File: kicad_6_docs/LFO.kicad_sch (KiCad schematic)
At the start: 13 parts, among them SW2 SW_SPDT, U14 SSI2164, U15 TL072

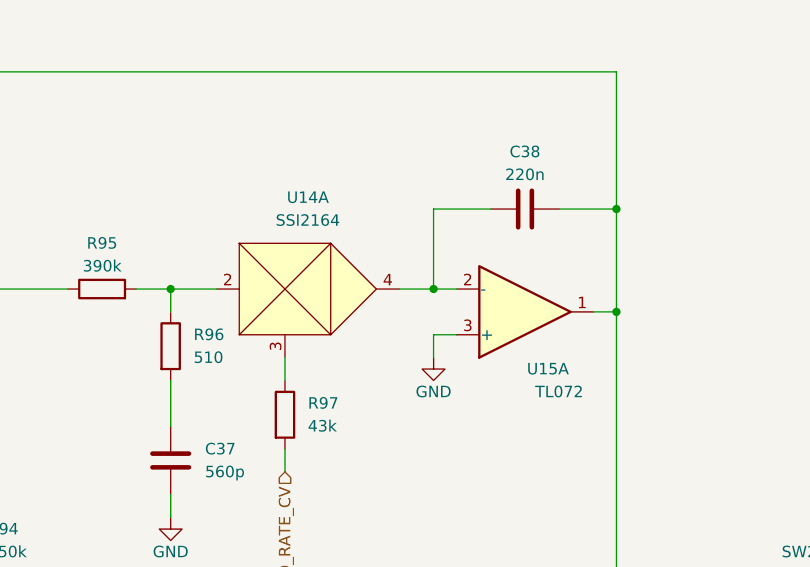
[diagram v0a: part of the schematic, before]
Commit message: Fix power supply errors, tidy up schematic
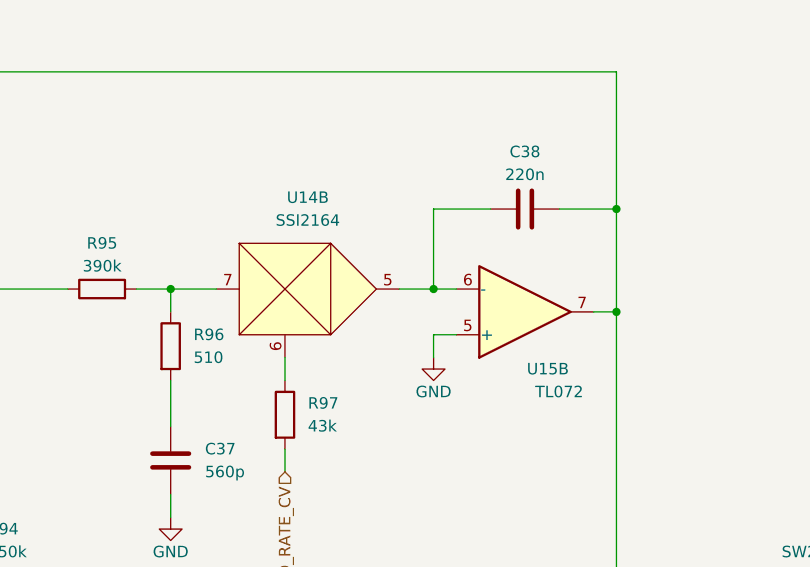
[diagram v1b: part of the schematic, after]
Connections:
- net GND: now also U15.5 (+); no longer U15.3 (+)
- net TRIANGLE: now also U15.7; no longer U15.1
- net at R97.1: now also U14.6; no longer U14.3
- net at R95.2, R96.1: now also U14.7; no longer U14.2
- new net: C38.1, U14.5, U15.6 (-)
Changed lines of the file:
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@@
   (title_block
     (title "Mu-Tron Bi-Phase near-clone")
-    (date "2022-01-14")
+    (date "2022-08-01")
     (rev "0")
     (comment 2 "creativecommons.org/licenses/by/4.0/")
@@
     (effects (font (size 1.27 1.27)) (justify left))
   )
-  (symbol (lib_id "Device:R") (at 148.59 101.6 0)
+  (symbol (lib_id "Device:R") (at 148.59 101.6 0) (unit 1)
     (in_bom yes) (on_board yes) (fields_autoplaced)
     (property "Reference" "R97" (id 0) (at 151.13 100.3299 0)
@@
     (pin "2")
   )
-  (symbol (lib_id "Amplifier_Operational:TL072") (at 175.26 90.17 0) (mirror x)
+  (symbol (lib_id "Amplifier_Operational:TL072") (at 175.26 90.17 0) (mirror x) (unit 2)
     (in_bom yes) (on_board yes)
     (property "Reference" "U15" (id 0) (at 177.8 96.52 0))
@@
       (effects (font (size 1.27 1.27)) hide)
     )
+    (pin "1")
+    (pin "2")
+    (pin "3")
     (pin "5")
     (pin "6")
     (pin "7")
-  )
-  (symbol (lib_id "Device:R") (at 96.52 76.2 90)
+    (pin "4")
+    (pin "8")
+  )
+  (symbol (lib_id "Device:R") (at 96.52 76.2 90) (unit 1)
     (in_bom yes) (on_board yes)
     (property "Reference" "R93" (id 0) (at 96.52 71.12 90))
@@
     (pin "2")
   )
-  (symbol (lib_id "custom_symbols:SSI2164") (at 148.59 87.63 0)
+  (symbol (lib_id "custom_symbols:SSI2164") (at 148.59 87.63 0) (unit 2)
     (in_bom yes) (on_board yes) (fields_autoplaced)
     (property "Reference" "U14" (id 0) (at 151.13 77.47 0))
@@
       (effects (font (size 1.27 1.27)) hide)
     )
+    (pin "2")
+    (pin "3")
+    (pin "4")
     (pin "5")
     (pin "6")
     (pin "7")
-  )
-  (symbol (lib_id "Device:C") (at 135.89 106.68 0)
+    (pin "10")
+    (pin "11")
+    (pin "12")
+    (pin "13")
+    (pin "14")
+    (pin "15")
+    (pin "1")
+    (pin "16")
+    (pin "8")
+    (pin "9")
+  )
+  (symbol (lib_id "Device:C") (at 135.89 106.68 0) (unit 1)
     (in_bom yes) (on_board yes) (fields_autoplaced)
     (property "Reference" "C37" (id 0) (at 139.7 105.4099 0)
@@
     (pin "2")
   )
-  (symbol (lib_id "Device:R") (at 113.03 115.57 0)
+  (symbol (lib_id "Device:R") (at 113.03 115.57 0) (unit 1)
     (in_bom yes) (on_board yes) (fields_autoplaced)
     (property "Reference" "R94" (id 0) (at 115.57 114.2999 0)
@@
     (pin "2")
   )
-  (symbol (lib_id "Device:C") (at 175.26 78.74 90)
+  (symbol (lib_id "Device:C") (at 175.26 78.74 90) (unit 1)
     (in_bom yes) (on_board yes)
     (property "Reference" "C38" (id 0) (at 175.26 72.39 90))
@@
     (pin "2")
   )
-  (symbol (lib_id "Device:C") (at 113.03 133.35 0)
+  (symbol (lib_id "Device:C") (at 113.03 133.35 0) (unit 1)
     (in_bom yes) (on_board yes) (fields_autoplaced)
     (property "Reference" "C36" (id 0) (at 116.84 132.0799 0)
@@
     (pin "2")
   )
-  (symbol (lib_id "Device:R") (at 135.89 93.98 0)
+  (symbol (lib_id "Device:R") (at 135.89 93.98 0) (unit 1)
     (in_bom yes) (on_board yes) (fields_autoplaced)
     (property "Reference" "R96" (id 0) (at 138.43 92.7099 0)
@@
     (pin "2")
   )
-  (symbol (lib_id "power:GND") (at 165.1 95.25 0)
+  (symbol (lib_id "power:GND") (at 165.1 95.25 0) (unit 1)
     (in_bom yes) (on_board yes)
     (property "Reference" "#PWR066" (id 0) (at 165.1 101.6 0)
@@
     (pin "1")
   )
-  (symbol (lib_id "power:GND") (at 86.36 92.71 0)
+  (symbol (lib_id "power:GND") (at 86.36 92.71 0) (unit 1)
     (in_bom yes) (on_board yes)
     (property "Reference" "#PWR063" (id 0) (at 86.36 99.06 0)
@@
     (pin "1")
   )
-  (symbol (lib_id "Amplifier_Operational:TL072") (at 96.52 87.63 0) (mirror x)
+  (symbol (lib_id "Amplifier_Operational:TL072") (at 96.52 87.63 0) (mirror x) (unit 1)
     (in_bom yes) (on_board yes)
     (property "Reference" "U15" (id 0) (at 99.06 93.98 0))
@@
     (pin "2")
     (pin "3")
-  )
-  (symbol (lib_id "power:GND") (at 135.89 113.03 0)
+    (pin "5")
+    (pin "6")
+    (pin "7")
+    (pin "4")
+    (pin "8")
+  )
+  (symbol (lib_id "power:GND") (at 135.89 113.03 0) (unit 1)
     (in_bom yes) (on_board yes)
     (property "Reference" "#PWR065" (id 0) (at 135.89 119.38 0)
@@
     (pin "1")
   )
-  (symbol (lib_id "Switch:SW_SPDT") (at 205.74 124.46 0) (mirror y)
+  (symbol (lib_id "Switch:SW_SPDT") (at 205.74 124.46 0) (mirror y) (unit 1)
     (in_bom yes) (on_board yes) (fields_autoplaced)
     (property "Reference" "SW2" (id 0) (at 205.74 116.84 0))
@@
     (pin "3")
   )
-  (symbol (lib_id "Device:R") (at 128.27 87.63 90)
+  (symbol (lib_id "Device:R") (at 128.27 87.63 90) (unit 1)
     (in_bom yes) (on_board yes)
     (property "Reference" "R95" (id 0) (at 128.27 82.55 90))
@@
     (pin "2")
   )
-  (symbol (lib_id "Device:R") (at 96.52 63.5 90)
+  (symbol (lib_id "Device:R") (at 96.52 63.5 90) (unit 1)
     (in_bom yes) (on_board yes)
     (property "Reference" "R92" (id 0) (at 96.52 58.42 90))
@@
     (pin "2")
   )
-  (symbol (lib_id "power:GND") (at 113.03 139.7 0)
+  (symbol (lib_id "power:GND") (at 113.03 139.7 0) (unit 1)
     (in_bom yes) (on_board yes)
     (property "Reference" "#PWR064" (id 0) (at 113.03 146.05 0)
